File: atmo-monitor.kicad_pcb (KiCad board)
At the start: 2 copper layers, 60 x 69 mm, 27 parts, among them J1 E-Ink, J2 Power, J3 Qwiic, J4 PM Sensor, SW1 Reset, SW2 1825232-1, U1 STM32F103CBT6, U2 LP2950-3.3_TO252

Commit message: Finished initial design
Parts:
- removed J2: Power, custom_footprint:Adafruit Powerboost 500+
- added Q1: IRLML0100TRPbF, Package_TO_SOT_SMD:SOT-23, F.Cu at (123.5, 138.6)
- added U3: Power, custom_footprint:Adafruit Powerboost 500+, F.Cu at (148.1, 151.8)
- moved SW2 3.06 mm to (110.0, 89.5)
- moved H1 3.00 mm to (101.0, 91.0)
- moved H2 3.00 mm to (153.0, 91.0)
- moved J1 1.86 mm to (99.9, 135.6)
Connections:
- SW2 pad 1: LBO -> ENABLE
- U1 pad 10: unconnected-(U1-PA0-Pad10) -> MCU-LBO
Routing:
- net ENABLE: track 0.00 -> 90.2 mm, vias 0 -> 1
- net LBO: track 93.3 -> 13.0 mm, vias 1 -> 0
- net NRST: track 87.1 -> 112.5 mm, vias 5 -> 4
- net MCU-LBO: track 0.00 -> 22.9 mm
- net SWDIO: track 41.5 -> 62.1 mm
- net +3.3V: track 204.3 -> 219.6 mm, vias 6 -> 7
- net BUSY: track 68.5 -> 70.5 mm
- net ENA: track 72.6 -> 74.5 mm
- net SRCS: track 48.8 -> 46.9 mm
- net RST: track 67.0 -> 68.7 mm
- net D/C: track 19.1 -> 17.9 mm
- net SCK: track 13.6 -> 12.4 mm
- net ECS: track 17.6 -> 16.4 mm
- net GND: track 45.3 -> 44.3 mm
- net MOSI: track 19.5 -> 18.7 mm
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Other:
- board size 60 x 69 mm -> 60 x 66 mm

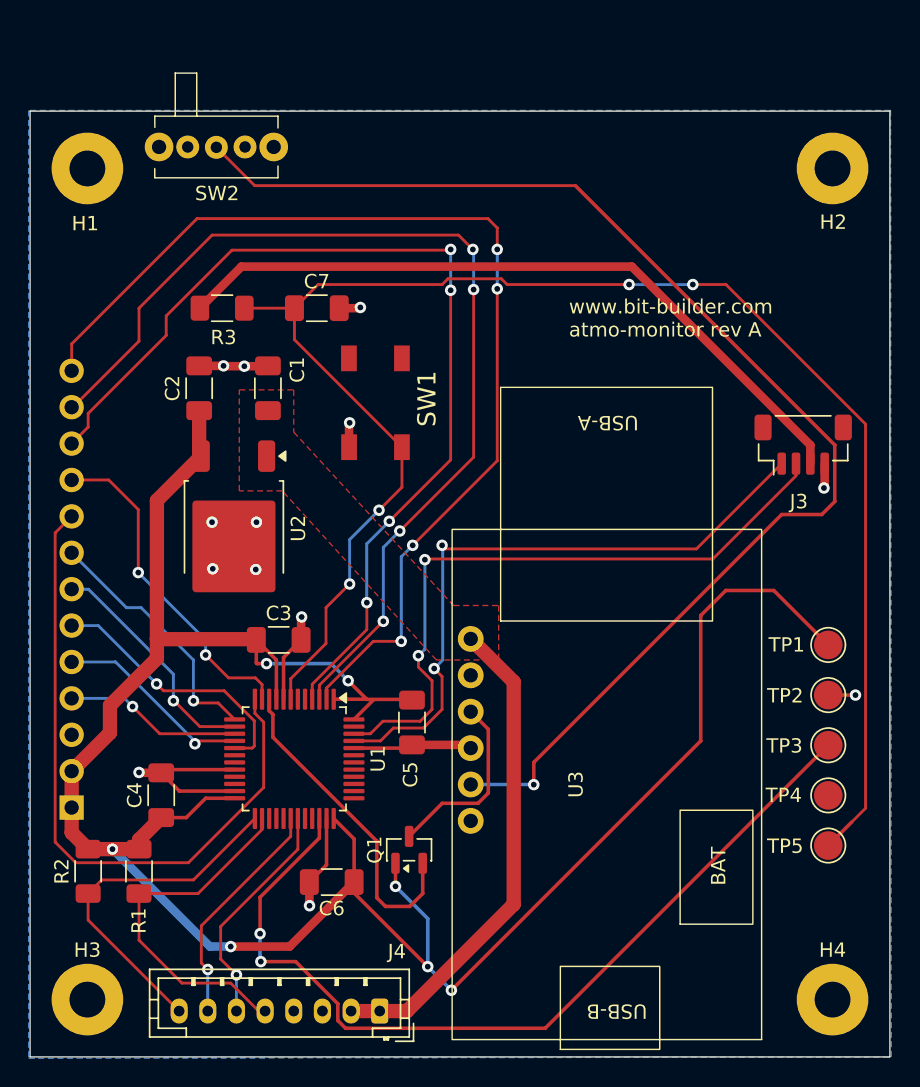
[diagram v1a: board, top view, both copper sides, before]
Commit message: Moved 2 signals from output limited ports
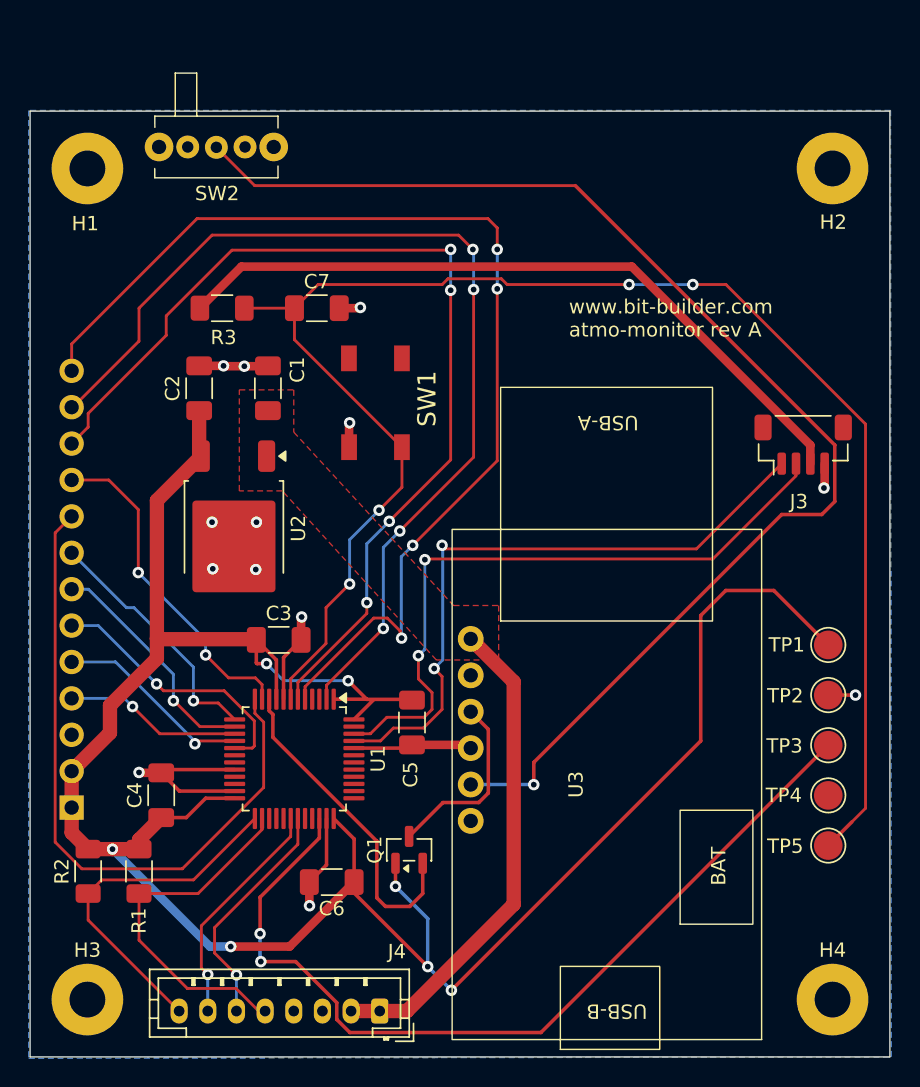
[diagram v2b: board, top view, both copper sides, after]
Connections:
- U1 pad 2: ENA -> BUSY
- U1 pad 3: BUSY -> unconnected-(U1-PC14-Pad3)
- U1 pad 4: RST -> unconnected-(U1-PC15-Pad4)
- U1 pad 5: unconnected-(U1-PD0-Pad5) -> ENA
- U1 pad 6: unconnected-(U1-PD1-Pad6) -> RST
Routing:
- net ENA: track 74.5 -> 77.3 mm

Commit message: Added R4 for SWCLK
Reordered debug test points
Fixed schematic DRC problems
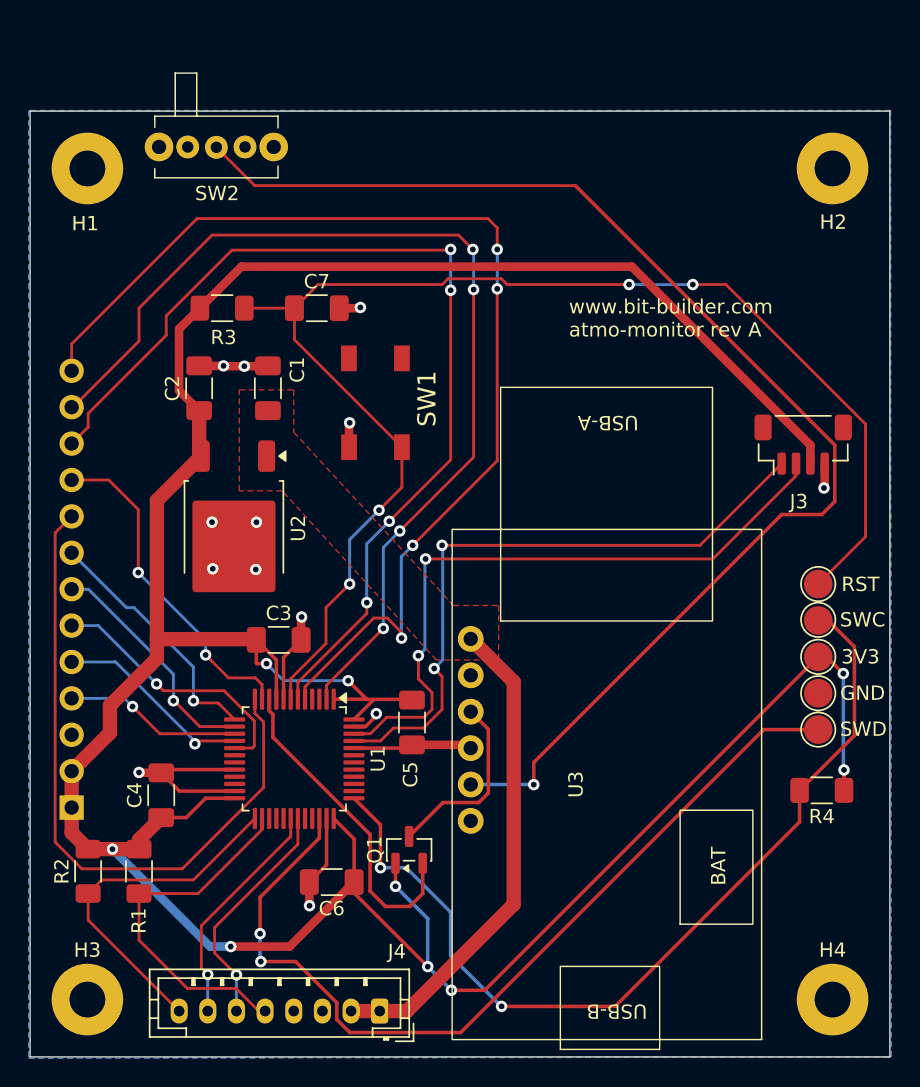
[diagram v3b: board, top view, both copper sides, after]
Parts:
- added R4: 10K, Resistor_SMD:R_1206_3216Metric_Pad1.30x1.75mm_HandSolder, F.Cu at (152.2, 134.4)
- TP1: value TestPoint -> 3V3
- TP2: value TestPoint -> GND
- TP3: value TestPoint -> SWD
- TP4: value TestPoint -> SWC
- TP5: value TestPoint -> RST
- moved TP5 18.3 mm to (152.0, 120.0)
- moved TP4 12.3 mm to (152.0, 122.5)
- moved TP3 1.30 mm to (152.0, 130.2)
- moved TP1 1.09 mm to (152.0, 125.1)
- moved TP2 0.71 mm to (152.0, 127.6)
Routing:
- net SWCLK: track 0.00 -> 62.4 mm, vias 0 -> 2
- net NRST: track 112.5 -> 94.5 mm
- net +3.3V: track 219.6 -> 228.5 mm, vias 7 -> 9

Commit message: Added R5 for LBO pull up on MCU
For proper level translation, need R5
Swapped RX and TX on PMS jumper so that it is legibly correct
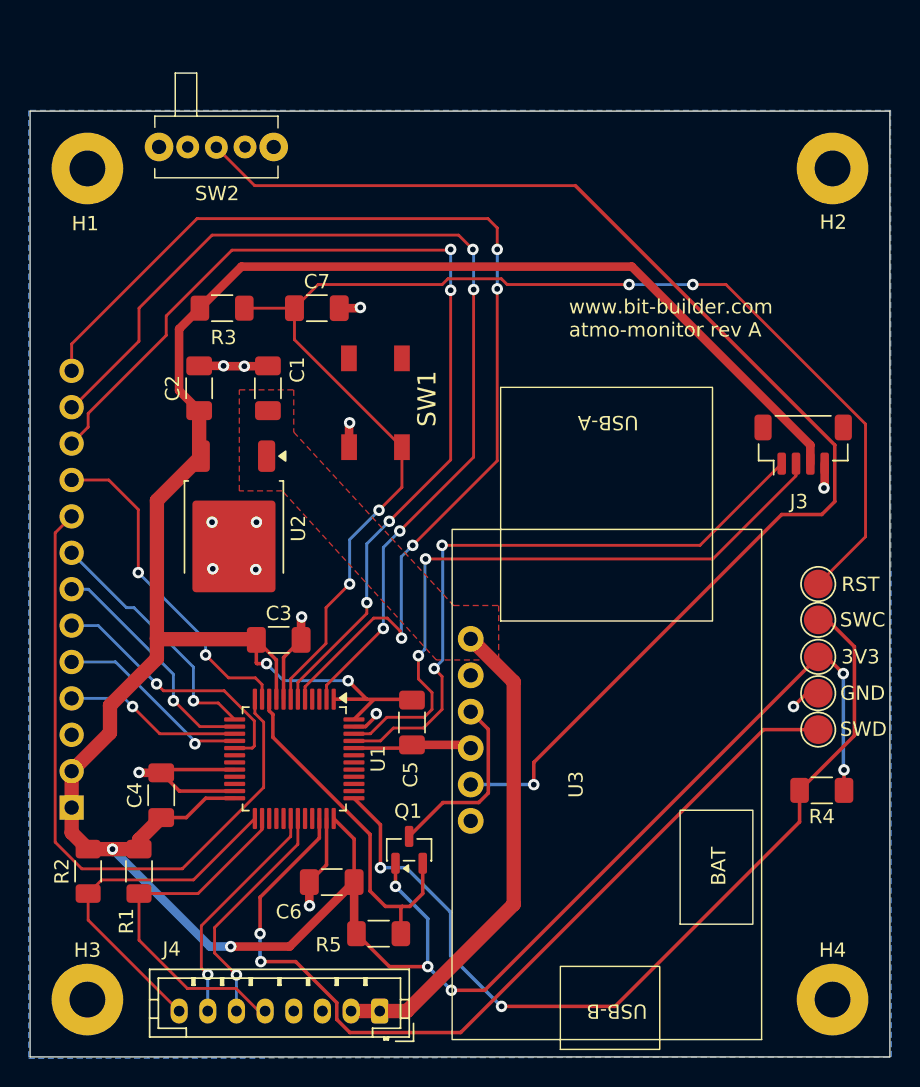
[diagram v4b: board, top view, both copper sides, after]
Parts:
- added R5: 10K, Resistor_SMD:R_1206_3216Metric_Pad1.30x1.75mm_HandSolder, F.Cu at (121.3, 144.4)
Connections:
- J4 pad 6: PM-RX -> PM-TX
- J4 pad 7: PM-TX -> PM-RX
- U1 pad 30: PM-TX -> PM-RX
- U1 pad 31: PM-RX -> PM-TX
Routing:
- net +3.3V: track 228.5 -> 230.8 mm
- net MCU-LBO: track 22.9 -> 24.8 mm
- net GND: track 44.4 -> 45.7 mm, vias 13 -> 14

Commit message: Updated trace routing for better clearance
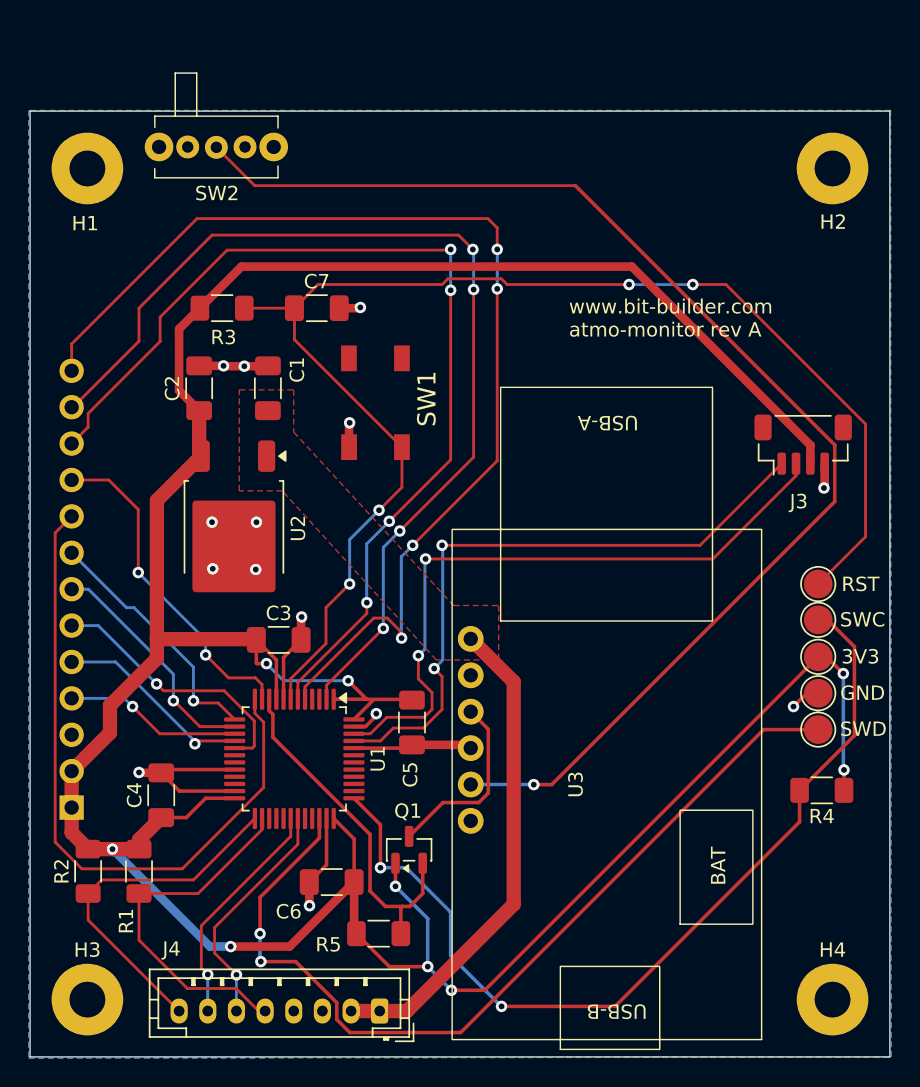
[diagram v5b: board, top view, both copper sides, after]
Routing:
- net ENABLE: track 90.2 -> 89.3 mm
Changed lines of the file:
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@@
 	)
 	(segment
-		(start 106.5 102.65)
-		(end 101.051 108.099)
+		(start 106.075 101.375)
+		(end 106.075 103.075)
+		(width 0.2)
+		(layer "F.Cu")
+		(net 9)
+	)
+	(segment
+		(start 115.6875 126.8625)
+		(end 115.6875 128.0375)
+		(width 0.2)
+		(layer "F.Cu")
+		(net 9)
+	)
+	(segment
+		(start 120.5 121.3)
+		(end 120.5 122.05)
+		(width 0.2)
+		(layer "F.Cu")
+		(net 9)
+	)
+	(segment
+		(start 101.051 108.099)
+		(end 101.051 109.049)
+		(width 0.2)
+		(layer "F.Cu")
+		(net 9)
+	)
+	(segment
+		(start 110.75 96.7)
+		(end 106.075 101.375)
+		(width 0.2)
+		(layer "F.Cu")
+		(net 9)
+	)
+	(segment
+		(start 126.35 99.5)
+		(end 126.35 111.336752)
 		(width 0.2)
 		(layer "F.Cu")
@@
 	)
 	(segment
-		(start 106.5 101.28884)
-		(end 106.5 102.65)
-		(width 0.2)
-		(layer "F.Cu")
-		(net 9)
-	)
-	(segment
-		(start 115.6875 126.8625)
-		(end 115.6875 128.0375)
-		(width 0.2)
-		(layer "F.Cu")
-		(net 9)
-	)
-	(segment
-		(start 120.5 121.3)
-		(end 120.5 122.05)
-		(width 0.2)
-		(layer "F.Cu")
-		(net 9)
-	)
-	(segment
 		(start 126.35 96.7)
-		(end 111.08884 96.7)
-		(width 0.2)
-		(layer "F.Cu")
-		(net 9)
-	)
-	(segment
-		(start 126.35 99.5)
-		(end 126.35 111.336752)
-		(width 0.2)
-		(layer "F.Cu")
-		(net 9)
-	)
-	(segment
-		(start 111.08884 96.7)
-		(end 106.5 101.28884)
-		(width 0.2)
-		(layer "F.Cu")
-		(net 9)
-	)
-	(segment
-		(start 101.051 108.099)
-		(end 101.051 109.049)
+		(end 110.75 96.7)
+		(width 0.2)
+		(layer "F.Cu")
+		(net 9)
+	)
+	(segment
+		(start 106.075 103.075)
+		(end 101.051 108.099)
 		(width 0.2)
 		(layer "F.Cu")
@@
 	)
 	(segment
-		(start 149.45 115.15)
-		(end 152.25 115.15)
-		(width 0.25)
-		(layer "F.Cu")
-		(net 17)
-	)
-	(segment
-		(start 132.15 132.45)
-		(end 149.45 115.15)
-		(width 0.25)
-		(layer "F.Cu")
-		(net 17)
-	)
-	(segment
 		(start 153.154486 110.301)
 		(end 135.051743 92.198257)
@@
 	)
 	(segment
+		(start 110 89.5254)
+		(end 112.672857 92.198257)
+		(width 0.2)
+		(layer "F.Cu")
+		(net 17)
+	)
+	(segment
+		(start 133.4 134)
+		(end 153.154486 114.245514)
+		(width 0.25)
+		(layer "F.Cu")
+		(net 17)
+	)
+	(segment
+		(start 112.672857 92.198257)
+		(end 135.051743 92.198257)
+		(width 0.2)
+		(layer "F.Cu")
+		(net 17)
+	)
+	(segment
+		(start 132.15 134)
+		(end 133.4 134)
+		(width 0.25)
+		(layer "F.Cu")
+		(net 17)
+	)
+	(segment
 		(start 153.154486 114.245514)
 		(end 153.154486 110.301)
 		(width 0.25)
 		(layer "F.Cu")
-		(net 17)
-	)
-	(segment
-		(start 110 89.5254)
-		(end 112.672857 92.198257)
-		(width 0.2)
-		(layer "F.Cu")
-		(net 17)
-	)
-	(segment
-		(start 152.25 115.15)
-		(end 153.154486 114.245514)
-		(width 0.25)
-		(layer "F.Cu")
-		(net 17)
-	)
-	(segment
-		(start 112.672857 92.198257)
-		(end 135.051743 92.198257)
-		(width 0.2)
-		(layer "F.Cu")
-		(net 17)
-	)
-	(segment
-		(start 132.15 134)
-		(end 132.15 132.45)
-		(width 0.25)
-		(layer "F.Cu")

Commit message: Finished schematic drc checks
Update pdb from schematic, no real changes
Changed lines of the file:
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@@
 			(net 32 "unconnected-(SW2-A-Pad3)")
 			(pinfunction "A")
-			(pintype "passive")
+			(pintype "passive+no_connect")
 		)
 		(pad "MN" thru_hole circle
@@
 			(net 19 "unconnected-(U1-PC14-Pad3)")
 			(pinfunction "PC14")
-			(pintype "bidirectional")
+			(pintype "bidirectional+no_connect")
 		)
 		(pad "4" smd roundrect
@@
 			(net 18 "unconnected-(U1-PC15-Pad4)")
 			(pinfunction "PC15")
-			(pintype "bidirectional")
+			(pintype "bidirectional+no_connect")
 		)
 		(pad "5" smd roundrect
@@
 			(net 26 "unconnected-(U1-PB0-Pad18)")
 			(pinfunction "PB0")
-			(pintype "bidirectional")
+			(pintype "bidirectional+no_connect")
 		)
 		(pad "19" smd roundrect
@@
 			(net 23 "unconnected-(U1-PB1-Pad19)")
 			(pinfunction "PB1")
-			(pintype "bidirectional")
+			(pintype "bidirectional+no_connect")
 		)
 		(pad "20" smd roundrect
@@
 			(net 21 "unconnected-(U1-PB10-Pad21)")
 			(pinfunction "PB10")
-			(pintype "bidirectional")
+			(pintype "bidirectional+no_connect")
 		)
 		(pad "22" smd roundrect
@@
 			(net 25 "unconnected-(U1-PB11-Pad22)")
 			(pinfunction "PB11")
-			(pintype "bidirectional")
+			(pintype "bidirectional+no_connect")
 		)
 		(pad "23" smd roundrect
@@
 			(net 20 "unconnected-(U1-PB14-Pad27)")
 			(pinfunction "PB14")
-			(pintype "bidirectional")
+			(pintype "bidirectional+no_connect")
 		)
 		(pad "28" smd roundrect
@@
 			(net 22 "unconnected-(U1-PB15-Pad28)")
 			(pinfunction "PB15")
-			(pintype "bidirectional")
+			(pintype "bidirectional+no_connect")
 		)
 		(pad "29" smd roundrect
@@
 			(net 37 "unconnected-(U1-PA8-Pad29)")
 			(pinfunction "PA8")
-			(pintype "bidirectional")
+			(pintype "bidirectional+no_connect")
 		)
 		(pad "30" smd roundrect
@@
 			(net 39 "unconnected-(U1-PA11-Pad32)")
 			(pinfunction "PA11")
-			(pintype "bidirectional")
+			(pintype "bidirectional+no_connect")
 		)
 		(pad "33" smd roundrect
@@
 			(net 40 "unconnected-(U1-PA12-Pad33)")
 			(pinfunction "PA12")
-			(pintype "bidirectional")
+			(pintype "bidirectional+no_connect")
 		)
 		(pad "34" smd roundrect
@@
 			(net 24 "unconnected-(U1-PA15-Pad38)")
 			(pinfunction "PA15")
-			(pintype "bidirectional")
+			(pintype "bidirectional+no_connect")
 		)
 		(pad "39" smd roundrect
@@
 			(net 42 "unconnected-(U1-PB3-Pad39)")
 			(pinfunction "PB3")
-			(pintype "bidirectional")
+			(pintype "bidirectional+no_connect")
 		)
 		(pad "40" smd roundrect
@@
 			(net 41 "unconnected-(U1-PB4-Pad40)")
 			(pinfunction "PB4")
-			(pintype "bidirectional")
+			(pintype "bidirectional+no_connect")
 		)
 		(pad "41" smd roundrect
@@
 			(net 43 "unconnected-(U1-PB5-Pad41)")
 			(pinfunction "PB5")
-			(pintype "bidirectional")
+			(pintype "bidirectional+no_connect")
 		)
 		(pad "42" smd roundrect
@@
 			(net 29 "unconnected-(U1-PB6-Pad42)")
 			(pinfunction "PB6")
-			(pintype "bidirectional")
+			(pintype "bidirectional+no_connect")
 		)
 		(pad "43" smd roundrect
@@
 			(net 38 "unconnected-(U1-PB7-Pad43)")
 			(pinfunction "PB7")
-			(pintype "bidirectional")
+			(pintype "bidirectional+no_connect")
 		)
 		(pad "44" smd roundrect
@@
 		(layer "F.Cu")
 		(net 1)
-	)
-	(segment
-		(start 119.6125 144.2375)
-		(end 119.775 144.4)
-		(width 0.6)
-		(layer "F.Cu")
-		(net 1)
